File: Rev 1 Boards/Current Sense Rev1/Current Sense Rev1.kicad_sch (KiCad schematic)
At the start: 0 parts

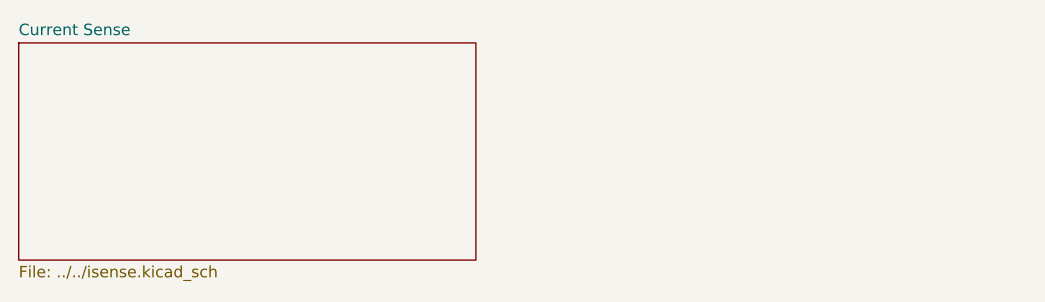
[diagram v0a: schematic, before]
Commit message: Correct symbol library path, renumber components
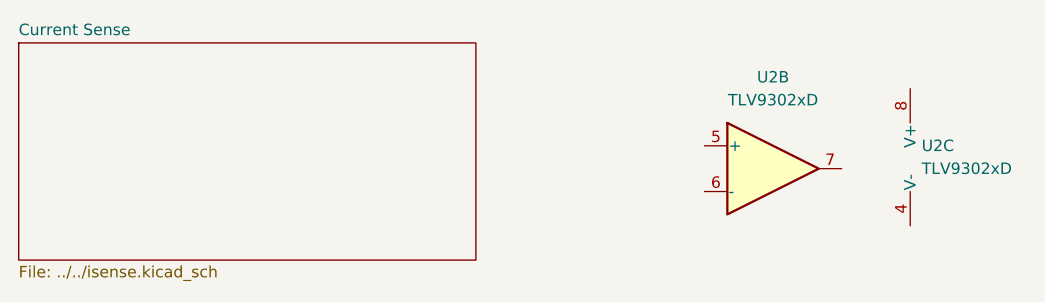
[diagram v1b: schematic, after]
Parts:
- added U2: TLV9302xD, Package_SO:SOIC-8_3.9x4.9mm_P1.27mm, symbol Amplifier_Operational:TLV9302xD
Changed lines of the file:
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@@
 	(generator_version "9.0")
 	(paper "A4")
+	(symbol
+		(lib_id "Amplifier_Operational:TLV9302xD")
+		(at 154.94 96.52 0)
+		(unit 2)
+		(exclude_from_sim no)
+		(in_bom yes)
+		(on_board yes)
+		(dnp no)
+		(fields_autoplaced yes)
+		(property "Reference" "U2"
+			(at 154.94 86.36 0)
+			(effects
+				(font
+					(size 1.27 1.27)
+				)
+			)
+		)
+		(property "Value" "TLV9302xD"
+			(at 154.94 88.9 0)
+			(effects
+				(font
+					(size 1.27 1.27)
+				)
+			)
+		)
+		(property "Footprint" "Package_SO:SOIC-8_3.9x4.9mm_P1.27mm"
+			(at 154.94 86.36 0)
+			(effects
+				(font
+					(size 1.27 1.27)
+				)
+				(hide yes)
+			)
+		)
+		(property "Datasheet" "https://www.ti.com/lit/ds/symlink/tlv9302.pdf"
+			(at 154.94 105.41 0)
+			(effects
+				(font
+					(size 1.27 1.27)
+				)
+				(hide yes)
+			)
+		)
+		(property "Description" "40-V, 1-MHz, RRO Operational Amplifiers for Cost-Sensitive Systems, SOIC-8"
+			(at 154.94 96.52 0)
+			(effects
+				(font
+					(size 1.27 1.27)
+				)
+				(hide yes)
+			)
+		)
+		(pin "6"
+		)
+		(pin "1"
+		)
+		(pin "2"
+		)
+		(pin "8"
+		)
+		(pin "3"
+		)
+		(pin "7"
+		)
+		(pin "4"
+		)
+		(pin "5"
+		)
+		(instances
+			(project "Current Sense Rev1"
+				(path "/d149d1fa-5de7-4dc0-b1ef-e9c4223d2865"
+					(reference "U2")
+					(unit 2)
+				)
+			)
+		)
+	)
+	(symbol
+		(lib_id "Amplifier_Operational:TLV9302xD")
+		(at 172.72 95.25 0)
+		(unit 3)
+		(exclude_from_sim no)
+		(in_bom yes)
+		(on_board yes)
+		(dnp no)
+		(fields_autoplaced yes)
+		(property "Reference" "U2"
+			(at 171.45 93.9799 0)
+			(effects
+				(font
+					(size 1.27 1.27)
+				)
+				(justify left)
+			)
+		)
+		(property "Value" "TLV9302xD"
+			(at 171.45 96.5199 0)
+			(effects
+				(font
+					(size 1.27 1.27)
+				)
+				(justify left)
+			)
+		)
+		(property "Footprint" "Package_SO:SOIC-8_3.9x4.9mm_P1.27mm"
+			(at 172.72 85.09 0)
+			(effects
+				(font
+					(size 1.27 1.27)
+				)
+				(hide yes)
+			)
+		)
+		(property "Datasheet" "https://www.ti.com/lit/ds/symlink/tlv9302.pdf"
+			(at 172.72 104.14 0)
+			(effects
+				(font
+					(size 1.27 1.27)
+				)
+				(hide yes)
+			)
+		)
+		(property "Description" "40-V, 1-MHz, RRO Operational Amplifiers for Cost-Sensitive Systems, SOIC-8"
+			(at 172.72 95.25 0)
+			(effects
+				(font
+					(size 1.27 1.27)
+				)
+				(hide yes)
+			)
+		)
+		(pin "6"
+		)
+		(pin "1"
+		)
+		(pin "2"
+		)
+		(pin "8"
+		)
+		(pin "3"
+		)
+		(pin "7"
+		)
+		(pin "4"
+		)
+		(pin "5"
+		)
+		(instances
+			(project "Current Sense Rev1"
+				(path "/d149d1fa-5de7-4dc0-b1ef-e9c4223d2865"
+					(reference "U2")
+					(unit 3)
+				)
+			)
+		)
+	)
 	(sheet
 		(at 71.12 82.55)

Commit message: Fix broken component links
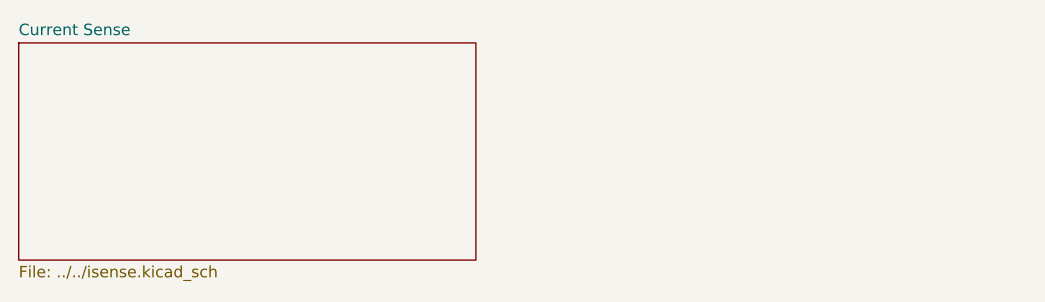
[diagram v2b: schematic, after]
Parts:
- removed U2: TLV9302xD, Package_SO:SOIC-8_3.9x4.9mm_P1.27mm, symbol Amplifier_Operational:TLV9302xD
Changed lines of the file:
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@@
 	(generator_version "9.0")
 	(paper "A4")
-	(symbol
-		(lib_id "Amplifier_Operational:TLV9302xD")
-		(at 154.94 96.52 0)
-		(unit 2)
-		(exclude_from_sim no)
-		(in_bom yes)
-		(on_board yes)
-		(dnp no)
-		(fields_autoplaced yes)
-		(property "Reference" "U2"
-			(at 154.94 86.36 0)
-			(effects
-				(font
-					(size 1.27 1.27)
-				)
-			)
-		)
-		(property "Value" "TLV9302xD"
-			(at 154.94 88.9 0)
-			(effects
-				(font
-					(size 1.27 1.27)
-				)
-			)
-		)
-		(property "Footprint" "Package_SO:SOIC-8_3.9x4.9mm_P1.27mm"
-			(at 154.94 86.36 0)
-			(effects
-				(font
-					(size 1.27 1.27)
-				)
-				(hide yes)
-			)
-		)
-		(property "Datasheet" "https://www.ti.com/lit/ds/symlink/tlv9302.pdf"
-			(at 154.94 105.41 0)
-			(effects
-				(font
-					(size 1.27 1.27)
-				)
-				(hide yes)
-			)
-		)
-		(property "Description" "40-V, 1-MHz, RRO Operational Amplifiers for Cost-Sensitive Systems, SOIC-8"
-			(at 154.94 96.52 0)
-			(effects
-				(font
-					(size 1.27 1.27)
-				)
-				(hide yes)
-			)
-		)
-		(pin "6"
-		)
-		(pin "1"
-		)
-		(pin "2"
-		)
-		(pin "8"
-		)
-		(pin "3"
-		)
-		(pin "7"
-		)
-		(pin "4"
-		)
-		(pin "5"
-		)
-		(instances
-			(project "Current Sense Rev1"
-				(path "/d149d1fa-5de7-4dc0-b1ef-e9c4223d2865"
-					(reference "U2")
-					(unit 2)
-				)
-			)
-		)
-	)
-	(symbol
-		(lib_id "Amplifier_Operational:TLV9302xD")
-		(at 172.72 95.25 0)
-		(unit 3)
-		(exclude_from_sim no)
-		(in_bom yes)
-		(on_board yes)
-		(dnp no)
-		(fields_autoplaced yes)
-		(property "Reference" "U2"
-			(at 171.45 93.9799 0)
-			(effects
-				(font
-					(size 1.27 1.27)
-				)
-				(justify left)
-			)
-		)
-		(property "Value" "TLV9302xD"
-			(at 171.45 96.5199 0)
-			(effects
-				(font
-					(size 1.27 1.27)
-				)
-				(justify left)
-			)
-		)
-		(property "Footprint" "Package_SO:SOIC-8_3.9x4.9mm_P1.27mm"
-			(at 172.72 85.09 0)
-			(effects
-				(font
-					(size 1.27 1.27)
-				)
-				(hide yes)
-			)
-		)
-		(property "Datasheet" "https://www.ti.com/lit/ds/symlink/tlv9302.pdf"
-			(at 172.72 104.14 0)
-			(effects
-				(font
-					(size 1.27 1.27)
-				)
-				(hide yes)
-			)
-		)
-		(property "Description" "40-V, 1-MHz, RRO Operational Amplifiers for Cost-Sensitive Systems, SOIC-8"
-			(at 172.72 95.25 0)
-			(effects
-				(font
-					(size 1.27 1.27)
-				)
-				(hide yes)
-			)
-		)
-		(pin "6"
-		)
-		(pin "1"
-		)
-		(pin "2"
-		)
-		(pin "8"
-		)
-		(pin "3"
-		)
-		(pin "7"
-		)
-		(pin "4"
-		)
-		(pin "5"
-		)
-		(instances
-			(project "Current Sense Rev1"
-				(path "/d149d1fa-5de7-4dc0-b1ef-e9c4223d2865"
-					(reference "U2")
-					(unit 3)
-				)
-			)
-		)
-	)
 	(sheet
 		(at 71.12 82.55)
